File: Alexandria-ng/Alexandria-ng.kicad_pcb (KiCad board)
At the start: 4 copper layers, 87 parts, among them J1 Eth0, J10 PoE3, J11 PoE4, J12 FFC, J13 +3.3V, J14 I²C, J2 Eth1, J3 Eth2, J4 Eth3, J5 Eth4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

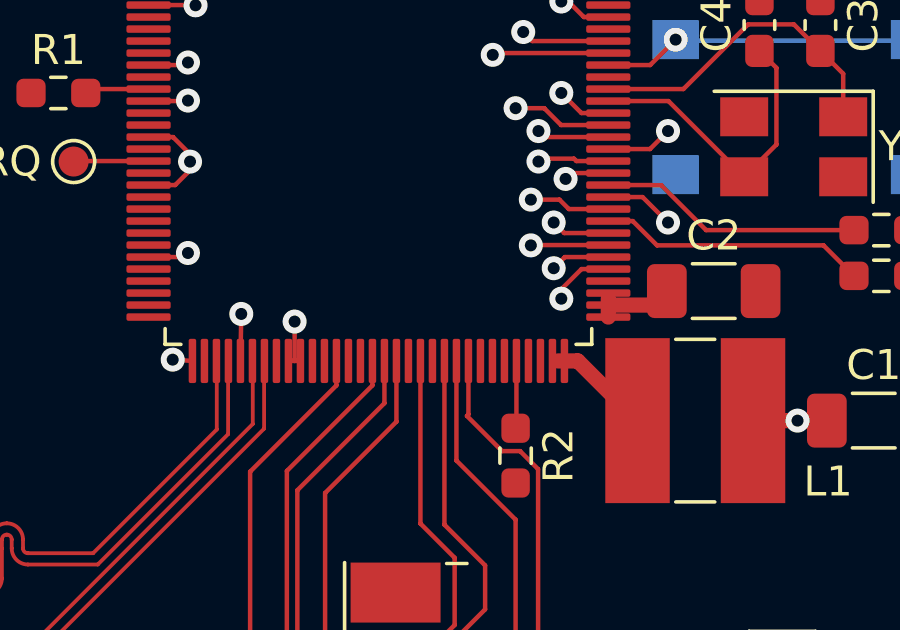
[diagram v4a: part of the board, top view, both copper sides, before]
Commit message: Switch DVDDIO pins to +2.8V
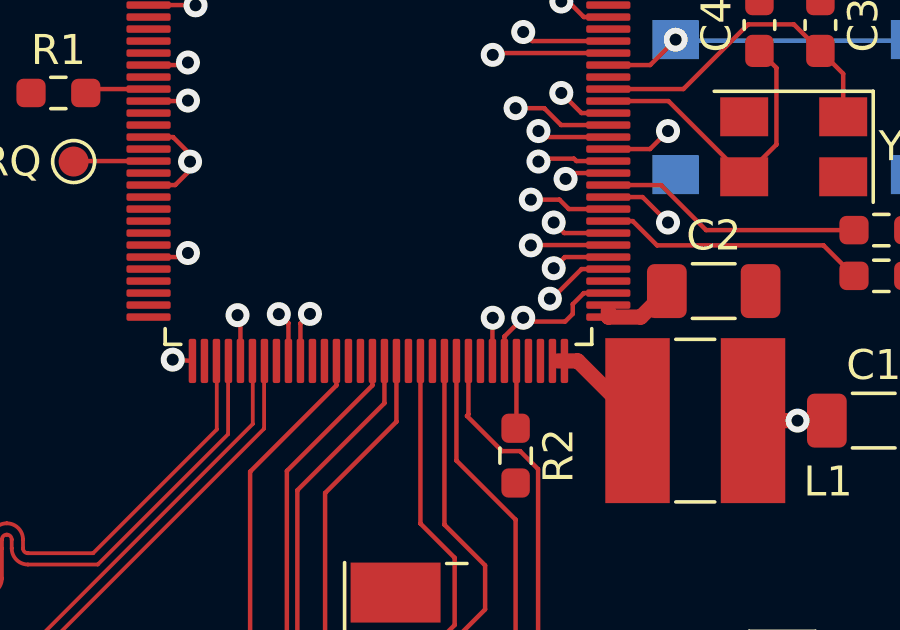
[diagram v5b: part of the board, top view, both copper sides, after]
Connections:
- J1 pad 10: +3.3V -> +2V8
- J2 pad 10: +3.3V -> +2V8
- J2 pad 12: +3.3V -> +2V8
- J3 pad 10: +3.3V -> +2V8
- J3 pad 12: +3.3V -> +2V8
- J4 pad 10: +3.3V -> +2V8
- J5 pad 10: +3.3V -> +2V8
- R11 pad 1: +3.3V -> +2V8
- R12 pad 1: +3.3V -> +2V8
- R13 pad 1: +3.3V -> +2V8
- R14 pad 1: +3.3V -> +2V8
- R15 pad 1: +3.3V -> +2V8
- R16 pad 1: +3.3V -> +2V8
- R3 pad 1: +3.3V -> +2V8
- R5 pad 1: +3.3V -> +2V8
- R7 pad 1: +3.3V -> +2V8
- R9 pad 1: +3.3V -> +2V8
- U1 pad 42: +3.3V -> +2V8
- U1 pad 59: +3.3V -> +2V8
- U1 pad 67: +3.3V -> +2V8
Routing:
- net +2V8: track 0.00 -> 25.7 mm, vias 0 -> 2
- net +3.3V: track 41.8 -> 22.3 mm
- net +1V1: track 15.1 -> 16.4 mm, vias 9 -> 10

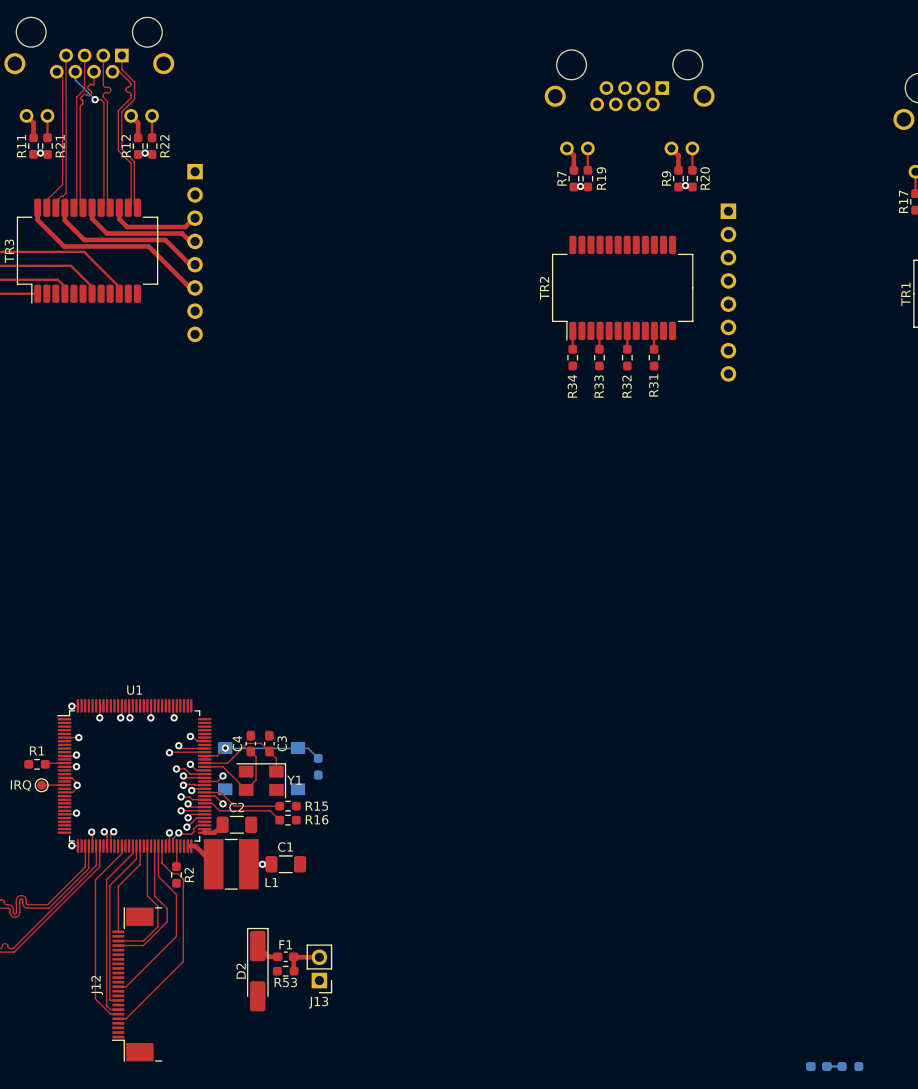
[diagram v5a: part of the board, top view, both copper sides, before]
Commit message: Balance vias on Ethernet jack, unroute RGMII (way too much skew)
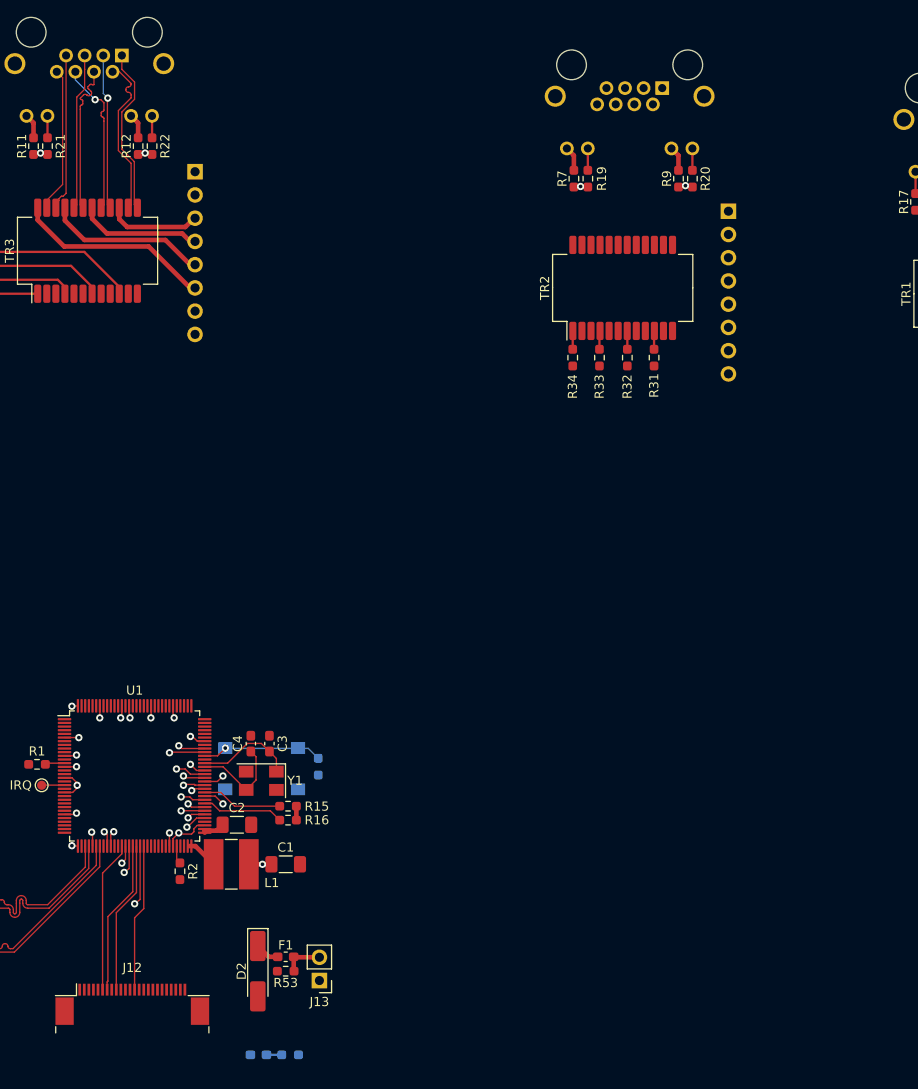
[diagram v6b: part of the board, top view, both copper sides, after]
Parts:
- moved D1 61.3 mm to (165.9, 142.2)
- moved R4 61.3 mm to (169.4, 142.2)
- moved J12 2.17 mm to (152.1, 136.7), turned to 0 degrees
- moved R2 0.56 mm to (157.4, 122.2)
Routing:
- net RG_RxD3: track 23.7 -> 0.00 mm
- net RG_RxD2: track 19.3 -> 0.00 mm
- net RG_RxCLK: track 0.00 -> 16.1 mm
- net RG_RxD1: track 15.3 -> 0.00 mm
- net RG_RxCTL: track 14.2 -> 0.00 mm
- net RG_TxD3: track 21.1 -> 16.6 mm
- net RG_TxCLK: track 10.4 -> 6.73 mm, vias 0 -> 1
- net RG_TxD1: track 0.00 -> 3.43 mm, vias 0 -> 1
- net RG_TxD0: track 20.1 -> 16.9 mm
- net RG_TxCTL: track 19.0 -> 16.6 mm
- net RG_TxD2: track 0.00 -> 2.30 mm, vias 0 -> 1
- net +2V8: track 25.7 -> 27.2 mm
- net P2BP: track 18.0 -> 17.0 mm, vias 0 -> 1

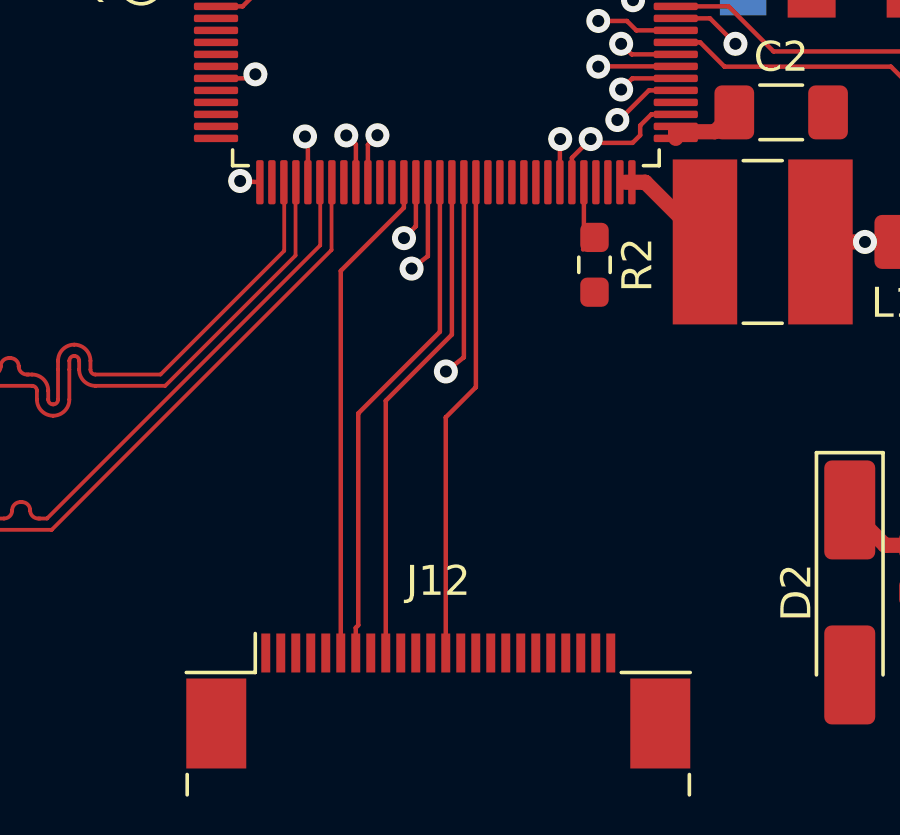
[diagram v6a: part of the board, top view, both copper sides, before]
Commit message: Finally routed RGMII with length matching
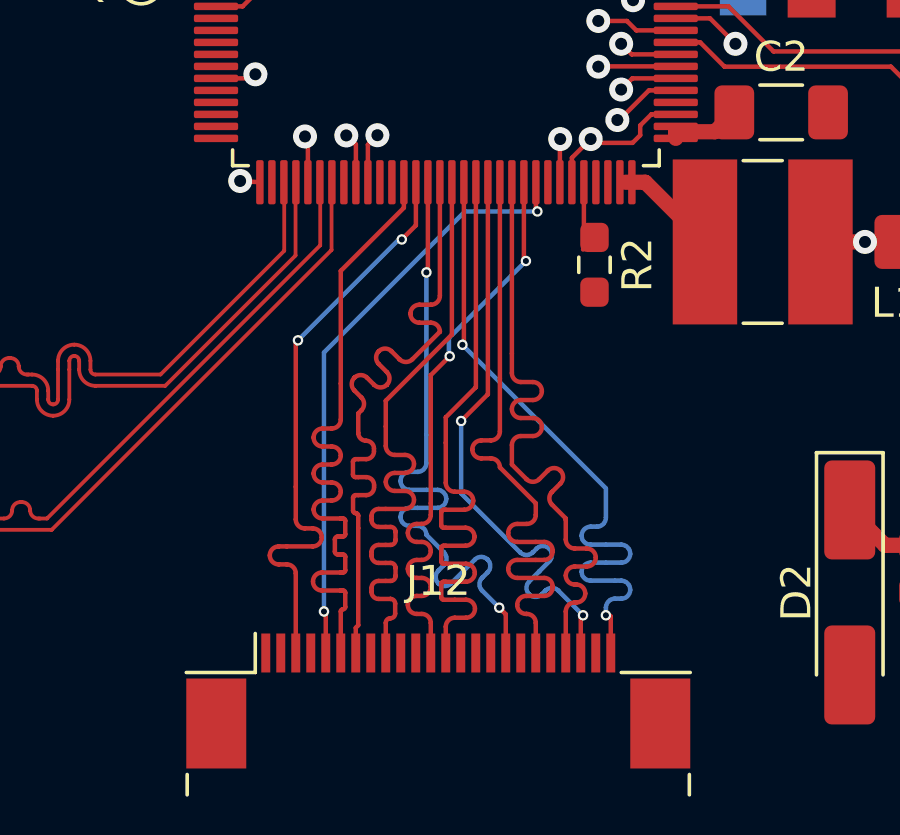
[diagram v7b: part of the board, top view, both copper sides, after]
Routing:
- net RG_RxD0: track 0.00 -> 23.0 mm
- net RG_RxD1: track 0.00 -> 22.9 mm
- net RG_RxD3: track 0.00 -> 20.1 mm, vias 0 -> 2
- net RG_RxCTL: track 0.00 -> 20.0 mm, vias 0 -> 2
- net RG_RxD2: track 0.00 -> 20.0 mm, vias 0 -> 2
- net RG_TxD1: track 3.43 -> 23.2 mm, vias 1 -> 2
- net RG_TxD2: track 2.30 -> 20.0 mm, vias 1 -> 2
- net RG_TxCLK: track 6.73 -> 23.0 mm, vias 1 -> 2
- net RG_RxCLK: track 16.1 -> 23.0 mm
- net RG_TxD3: track 16.6 -> 23.0 mm
- net RG_TxCTL: track 16.6 -> 23.0 mm
- net RG_TxD0: track 16.9 -> 22.9 mm
